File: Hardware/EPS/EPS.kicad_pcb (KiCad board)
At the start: 4 copper layers, 85 x 85 mm, 124 parts, among them J1001 Conn_01x02, J101 Conn_02x02_Odd_Even, J1101 Conn_01x02, J201 Conn_ARM_JTAG_SWD_10, J301 Conn_02x02_Counter_Clockwise, J401 USB_C_Receptacle_PowerOnly_6P, J601 Conn_02x20_Odd_Even, J701 Conn_01x02, J801 Conn_01x02, J901 Conn_01x02, M1201 MountingHole_Pad, M1202 MountingHole_Pad, M1203 MountingHole_Pad, M1204 MountingHole_Pad, Q301 RQ3G100GNTB, Q302 RQ3G100GNTB, U201 STM32L431RCT, U202 HZ0805E601R-10, U301 LTC4162EUFD-L41#PBF, U401 AP7361C-33Y5-13, U501 RT8258GE, U502 TPS27081ADDCR, U503 RT8258GE, U504 B230A-13-F

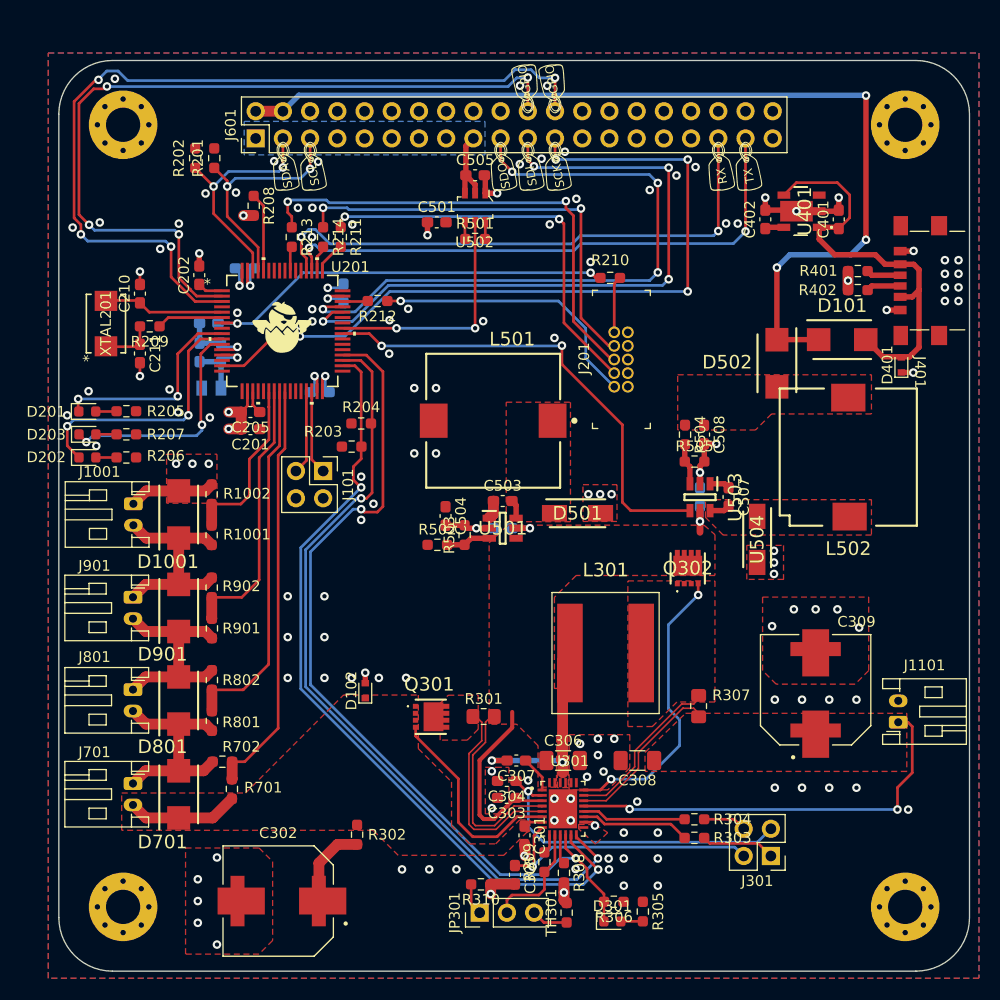
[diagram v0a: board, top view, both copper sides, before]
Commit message: Updated to KiCAD 7.0
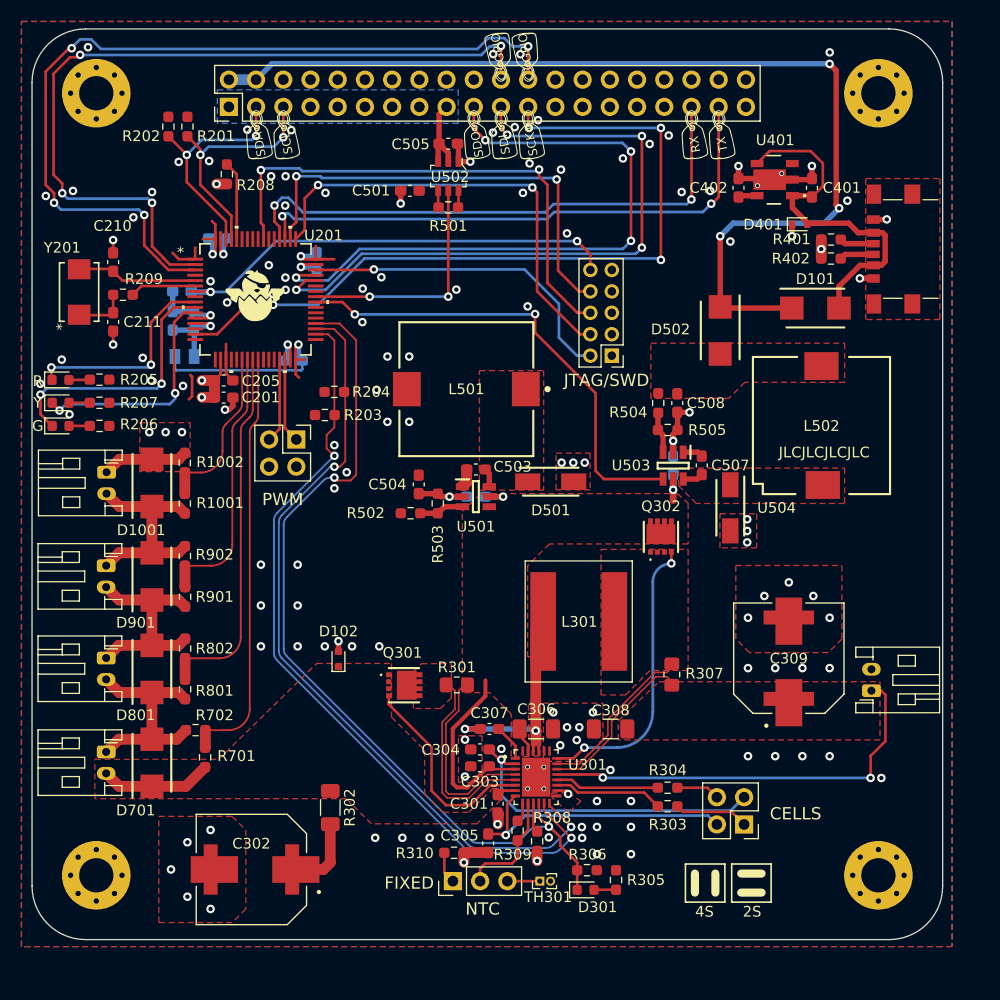
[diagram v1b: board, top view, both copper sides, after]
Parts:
- removed C206: 100nF, Capacitor_SMD:C_0603_1608Metric_Pad1.08x0.95mm_HandSolder
- removed the G002 at (122.9, 115.8)
- removed R210, R211, R212, R213, R214: 22, Resistor_SMD:R_0603_1608Metric_Pad0.98x0.95mm_HandSolder
- added G***: LOGO, graphics:torre_del_oro, B.Cu at (150.3, 110.0)
- C202: moved to B.Cu
- D203: value LED_B -> LED_YL
- J201: footprint digikey-footprints:PinHeader_2x5_P1.27mm_Drill.7mm -> Connector_PinHeader_2.00mm:PinHeader_2x05_P2.00mm_Vertical
- R1001, R701, R801, R901: value 100k -> 18k
- R1002, R702, R802, R902: value 100k -> 3.3k
- R302: value 2.5 -> 2.49; footprint Resistor_SMD:R_0603_1608Metric_Pad0.98x0.95mm_HandSolder -> Resistor_SMD:R_1206_3216Metric_Pad1.30x1.75mm_HandSolder
- TH301: footprint Resistor_SMD:R_0603_1608Metric_Pad0.98x0.95mm_HandSolder -> Connector_PinHeader_1.00mm:PinHeader_1x02_P1.00mm_Vertical
- moved D401 16.2 mm to (178.2, 75.6), turned to 0 degrees
- moved D502 6.12 mm to (170.8, 85.6)
- moved C303 3.87 mm to (148.4, 126.2)
- moved C305 3.87 mm to (149.1, 133.4)
- moved C504 3.87 mm to (142.7, 99.9)
- moved C506 3.87 mm to (148.0, 101.1)
- moved D301 3.87 mm to (158.2, 137.8)
- moved D701 3.87 mm to (117.8, 125.9)
- moved G001 3.87 mm to (177.1, 84.6)
- moved JP301 3.87 mm to (145.8, 137.0)
- moved L301 3.87 mm to (157.6, 112.7)
- moved R301 3.87 mm to (146.2, 118.6)
- moved R308 3.87 mm to (153.7, 133.2)
- moved TH301 3.87 mm to (154.0, 137.0)
- moved U501 3.87 mm to (148.0, 101.1)
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- renumbered XTAL201 to Y201
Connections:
- J201 pad 10: Net-(J201-Pad10) -> /STM32 MCU/NRST
- J201 pad 2: Net-(J201-Pad2) -> /STM32 MCU/JTMS
- J201 pad 4: Net-(J201-Pad4) -> /STM32 MCU/JTCK
- J201 pad 6: Net-(J201-Pad6) -> /STM32 MCU/JTDO
- J201 pad 8: Net-(J201-Pad8) -> /STM32 MCU/JTDI
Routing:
- net /STM32 MCU/JTDO: track 2.17 -> 48.8 mm, vias 0 -> 2
- net Net-(J201-Pad6): track 45.5 -> 0.00 mm, vias 2 -> 0
- net /STM32 MCU/JTDI: track 2.34 -> 42.9 mm, vias 0 -> 2
- net Net-(J201-Pad8): track 40.4 -> 0.00 mm, vias 2 -> 0
- net /STM32 MCU/JTCK: track 2.91 -> 42.5 mm, vias 0 -> 2
- net Net-(J201-Pad4): track 37.8 -> 0.00 mm, vias 2 -> 0
- net +3.3V: track 16.0 -> 46.1 mm, vias 33 -> 37
- net /STM32 MCU/JTMS: track 2.26 -> 30.8 mm, vias 0 -> 1
- net Net-(J201-Pad2): track 26.1 -> 0.00 mm, vias 1 -> 0
- net /USB Power/USB_VBUS: track 39.4 -> 32.9 mm
- net Net-(J201-Pad10): track 5.30 -> 0.00 mm
- net +5V: track 91.1 -> 95.9 mm
- net /STM32 MCU/NRST: track 39.5 -> 42.7 mm
- net GND: track 75.3 -> 74.2 mm, vias 116 -> 112
- net /STM32 MCU/ADC4: track 38.8 -> 39.5 mm
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- added copper zone on F.Cu, net unconnected-(J401-PadS1)
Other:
- board text added: "2S"
- board text added: "4S"
- board text added: "CELLS"
- board text added: "FIXED"
- board text added: "G"
- board text added: "JLCJLCJLCJLC"
- board text added: "JTAG/SWD"
- board text added: "NTC"
- board text added: "PWM"
- board text added: "R"
- board text added: "Y"
